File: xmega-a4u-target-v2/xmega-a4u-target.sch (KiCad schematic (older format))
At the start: 25 parts, among them CON1 USB-MINI-B, IC1 ATXMEGA128A4U-M, P1 PORTE, P2 PORTD, P3 PORTA, P4 PORTB, P5 PORTC, P6 PWR/RST, P7 PDI, U1 TSX-3225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

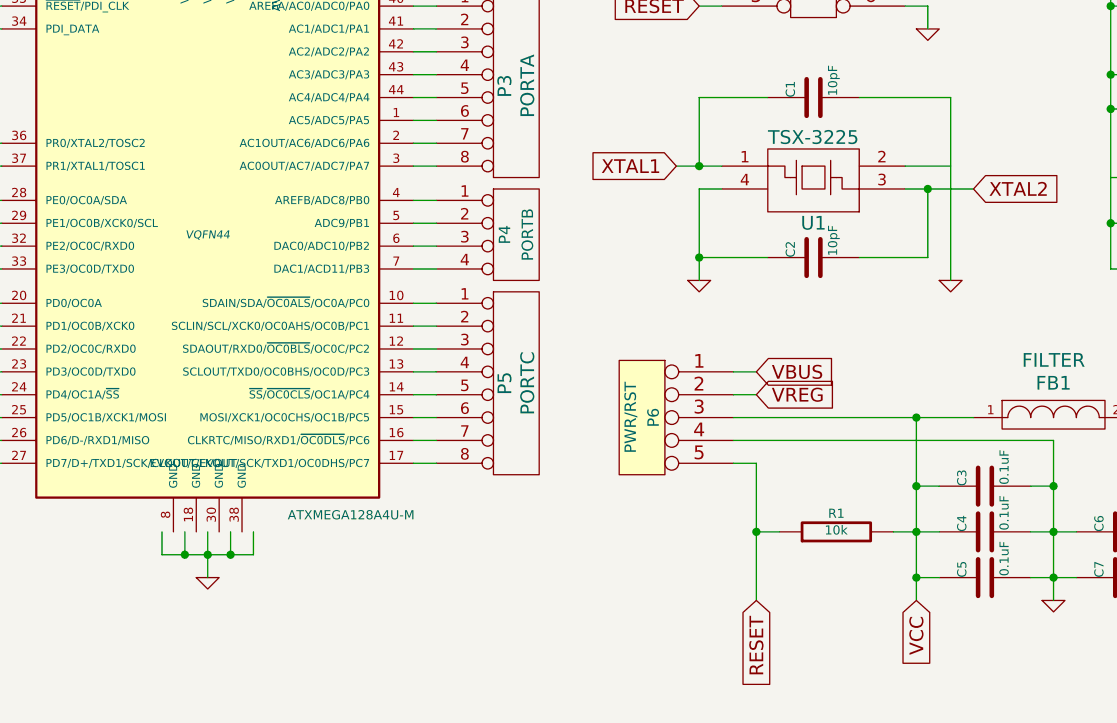
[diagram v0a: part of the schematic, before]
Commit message: fixed a mistake on XMEGA A4U board
one of the crystal's ground pads was not connected on the schematic
(the lines were "touching" but not actually connected)
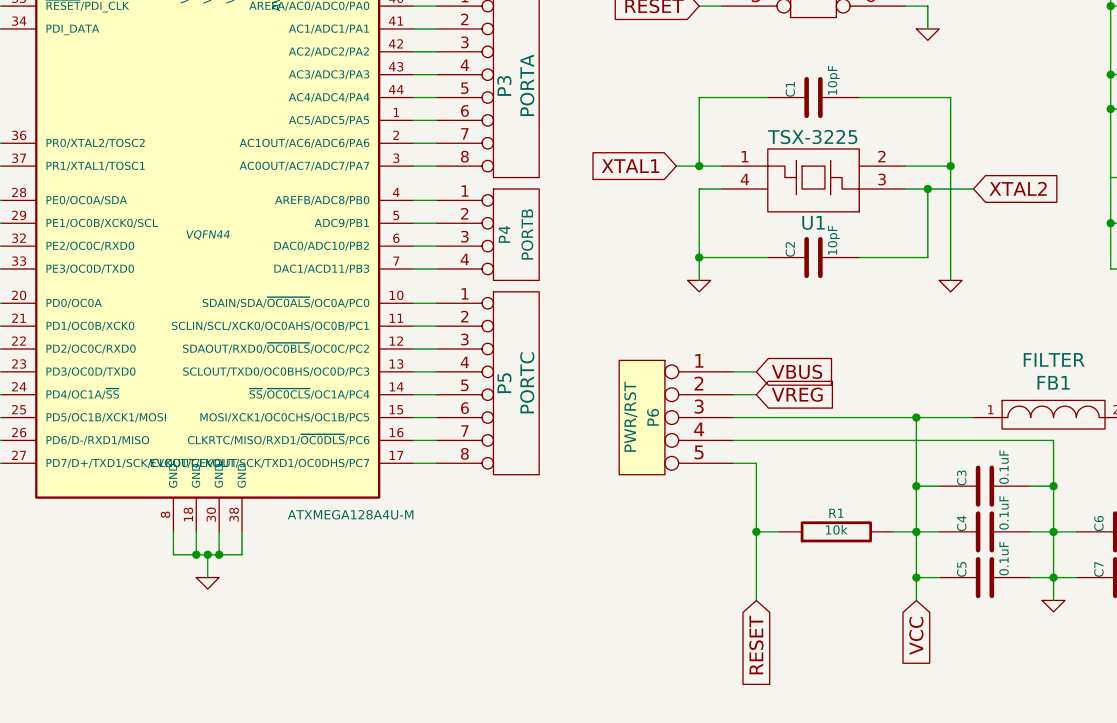
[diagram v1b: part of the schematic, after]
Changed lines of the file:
@@
 Sheet 1 1
 Title ""
-Date "20 jan 2014"
+Date "3 feb 2014"
 Rev ""
 Comp ""
@@
 	1050 3350 1350 3350
 Wire Wire Line
-	2050 3650 2050 3750
-Wire Wire Line
-	2050 3750 2450 3750
-Wire Wire Line
-	2350 3750 2350 3650
-Wire Wire Line
-	2250 3650 2250 3850
-Connection ~ 2250 3750
-Wire Wire Line
-	2150 3750 2150 3650
-Connection ~ 2150 3750
-Wire Wire Line
 	1250 1350 1350 1350
 Wire Wire Line
@@
 Wire Wire Line
 	5950 3250 4550 3250
-Wire Wire Line
-	2450 3750 2450 3650
-Connection ~ 2350 3750
+Connection ~ 5500 2050
+Wire Wire Line
+	2100 3650 2100 3750
+Wire Wire Line
+	2100 3750 2400 3750
+Wire Wire Line
+	2400 3750 2400 3650
+Wire Wire Line
+	2300 3650 2300 3750
+Connection ~ 2300 3750
+Wire Wire Line
+	2250 3750 2250 3850
+Connection ~ 2250 3750
+Wire Wire Line
+	2200 3750 2200 3650
+Connection ~ 2200 3750
 $EndSCHEMATC

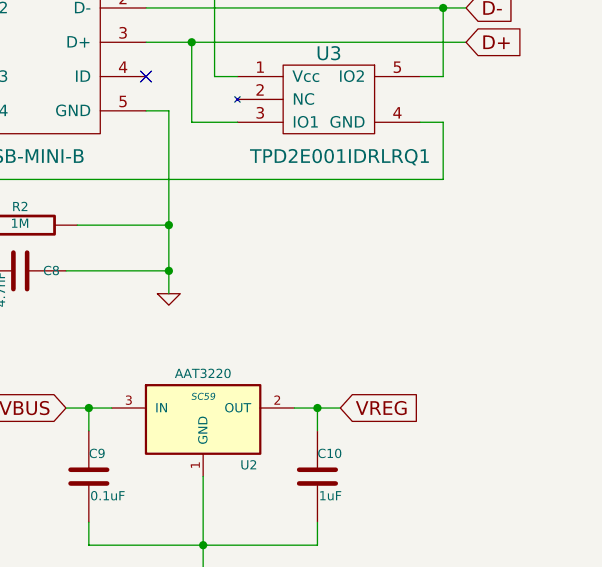
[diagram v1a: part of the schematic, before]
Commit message: embiggened pin header drill holes on A4U board...
... and added a VREG-VCC jumper
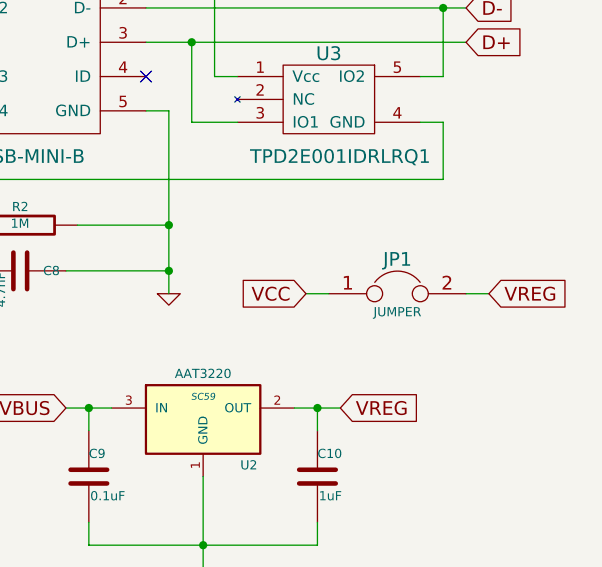
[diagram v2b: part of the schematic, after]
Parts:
- added JP1: JUMPER, ~, symbol JUMPER
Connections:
- net VCC: now also JP1.1
- net VREG: now also JP1.2
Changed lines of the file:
@@
 Sheet 1 1
 Title ""
-Date "3 feb 2014"
+Date "17 feb 2014"
 Rev ""
 Comp ""
@@
 $EndComp
 $Comp
-L GND #PWR01
+L GND #PWR2
 U 1 1 52DC5B10
 P 4400 2550
-F 0 "#PWR01" H 4400 2550 30  0001 C CNN
+F 0 "#PWR2" H 4400 2550 30  0001 C CNN
 F 1 "GND" H 4400 2480 30  0001 C CNN
 F 2 "" H 4400 2550 60  0000 C CNN
@@
 $EndComp
 $Comp
-L GND #PWR02
+L GND #PWR4
 U 1 1 52DC5B29
 P 5500 2550
-F 0 "#PWR02" H 5500 2550 30  0001 C CNN
+F 0 "#PWR4" H 5500 2550 30  0001 C CNN
 F 1 "GND" H 5500 2480 30  0001 C CNN
 F 2 "" H 5500 2550 60  0000 C CNN
@@
 $EndComp
 $Comp
-L GND #PWR03
+L GND #PWR1
 U 1 1 52DC64F1
 P 2250 3850
-F 0 "#PWR03" H 2250 3850 30  0001 C CNN
+F 0 "#PWR1" H 2250 3850 30  0001 C CNN
 F 1 "GND" H 2250 3780 30  0001 C CNN
 F 2 "" H 2250 3850 60  0000 C CNN
@@
 VCC
 $Comp
-L GND #PWR04
+L GND #PWR3
 U 1 1 52DC709C
 P 5400 1450
-F 0 "#PWR04" H 5400 1450 30  0001 C CNN
+F 0 "#PWR3" H 5400 1450 30  0001 C CNN
 F 1 "GND" H 5400 1380 30  0001 C CNN
 F 2 "" H 5400 1450 60  0000 C CNN
@@
 VBUS
 $Comp
-L GND #PWR05
+L GND #PWR6
 U 1 1 52DC76AE
 P 7500 2600
-F 0 "#PWR05" H 7500 2600 30  0001 C CNN
+F 0 "#PWR6" H 7500 2600 30  0001 C CNN
 F 1 "GND" H 7500 2530 30  0001 C CNN
 F 2 "" H 7500 2600 60  0000 C CNN
@@
 $EndComp
 $Comp
-L GND #PWR06
+L GND #PWR5
 U 1 1 52DC9B21
 P 5950 3950
-F 0 "#PWR06" H 5950 3950 30  0001 C CNN
+F 0 "#PWR5" H 5950 3950 30  0001 C CNN
 F 1 "GND" H 5950 3880 30  0001 C CNN
 F 2 "" H 5950 3950 60  0000 C CNN
@@
 Connection ~ 7650 3700
 $Comp
-L GND #PWR07
+L GND #PWR7
 U 1 1 52DCBB14
 P 7650 3800
-F 0 "#PWR07" H 7650 3800 30  0001 C CNN
+F 0 "#PWR7" H 7650 3800 30  0001 C CNN
 F 1 "GND" H 7650 3730 30  0001 C CNN
 F 2 "" H 7650 3800 60  0000 C CNN
@@
 	2200 3750 2200 3650
 Connection ~ 2200 3750
+$Comp
+L JUMPER JP1
+U 1 1 530271F2
+P 8500 2600
+F 0 "JP1" H 8500 2750 60  0000 C CNN
+F 1 "JUMPER" H 8500 2520 40  0000 C CNN
+F 2 "~" H 8500 2600 60  0000 C CNN
+F 3 "~" H 8500 2600 60  0000 C CNN
+	1    8500 2600
+	1    0    0    -1
+$EndComp
+Text GLabel 8900 2600 2    60   Input ~ 0
+VREG
+Text GLabel 8100 2600 0    60   Input ~ 0
+VCC
+Wire Wire Line
+	8900 2600 8800 2600
+Wire Wire Line
+	8200 2600 8100 2600
 $EndSCHEMATC
